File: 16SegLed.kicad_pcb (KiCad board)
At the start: 2 copper layers, 99.9 x 79.6 mm, 57 parts, among them J1 Conn_01x10, J2 Conn_01x10, J3 Conn_01x10, J4 Conn_01x06_Socket, J5 Conn_01x04_Pin, J6 Conn_01x04_Pin, Q1 BSS138, Q2 BSS138, SW1 SW_Push, SW2 SW_Push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

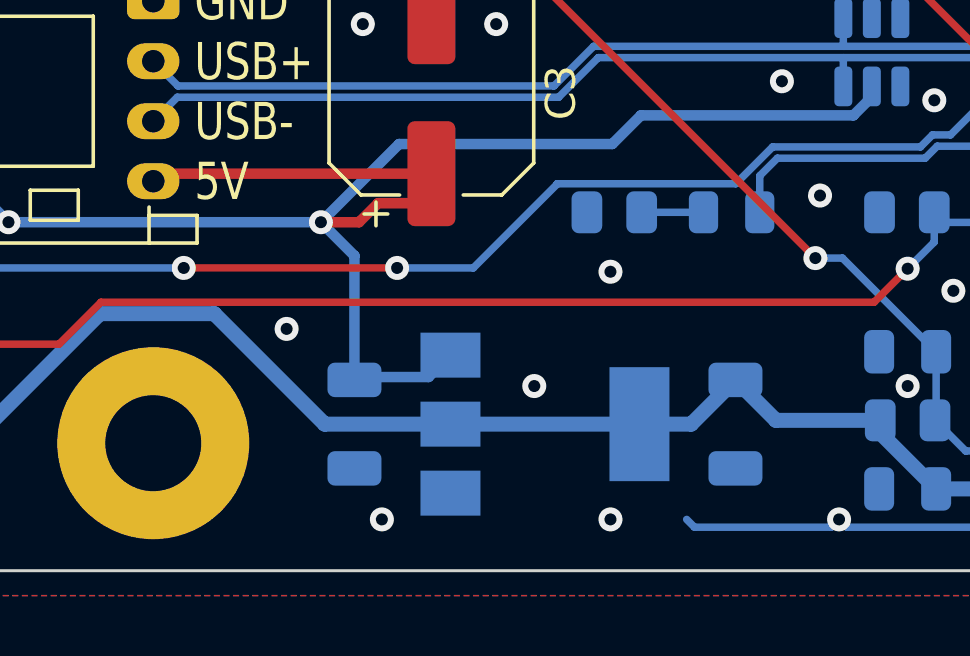
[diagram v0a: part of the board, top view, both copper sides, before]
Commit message: Fix 3.3 V regulator circuit
- Use polarized footprints for tantalum capacitors
- Add 100nF at input and output of AMS1117
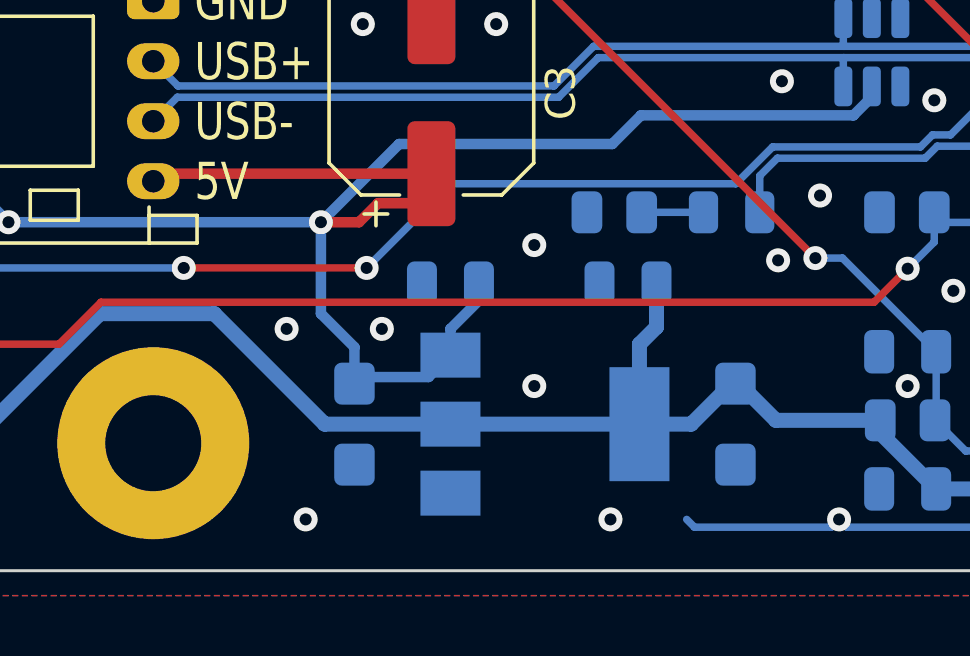
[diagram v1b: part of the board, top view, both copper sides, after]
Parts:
- added C10: 100nF, Capacitor_SMD:C_0805_2012Metric, B.Cu at (166.6, 163.2)
- added C11: 100nF, Capacitor_SMD:C_0805_2012Metric, B.Cu at (160.7, 163.2)
- C4, C5: footprint Capacitor_SMD:C_1206_3216Metric -> Capacitor_Tantalum_SMD:CP_EIA-3216-10_Kemet-I
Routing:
- net +3V3: track 121.5 -> 126.5 mm
- net +5V: track 200.0 -> 202.8 mm
- net GND: vias 96 -> 98

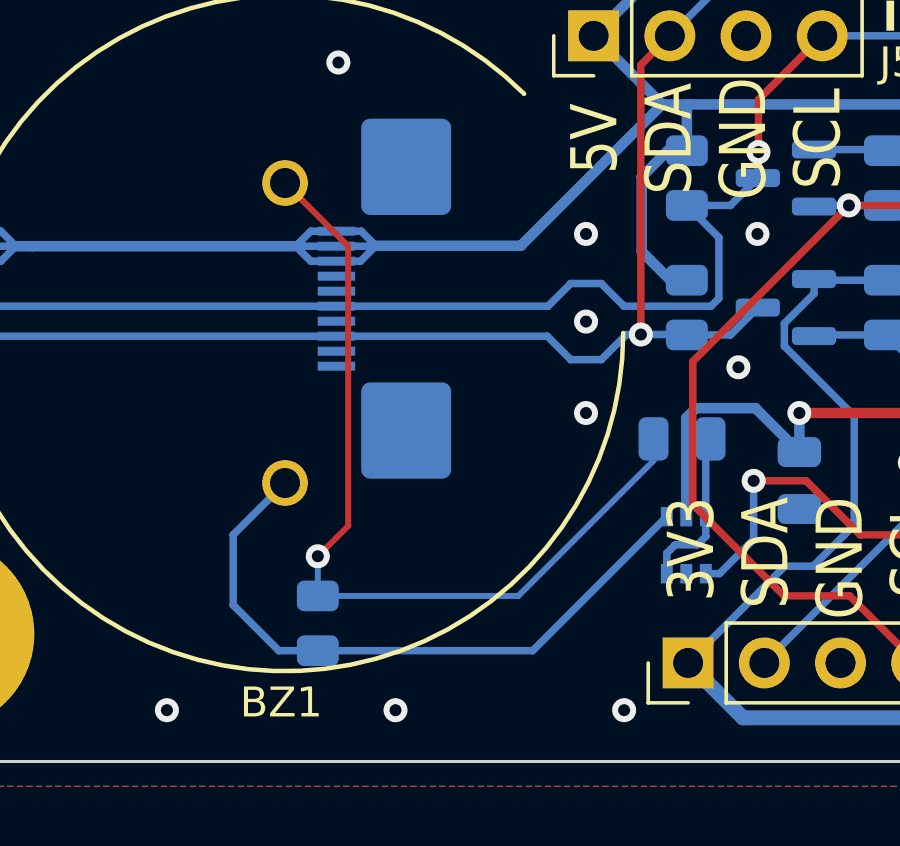
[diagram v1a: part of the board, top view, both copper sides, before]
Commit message: Add boxes to component groups on silkscreen
- including rearrangement of piezo buzzer's discharge resistor closer to other parts of that group
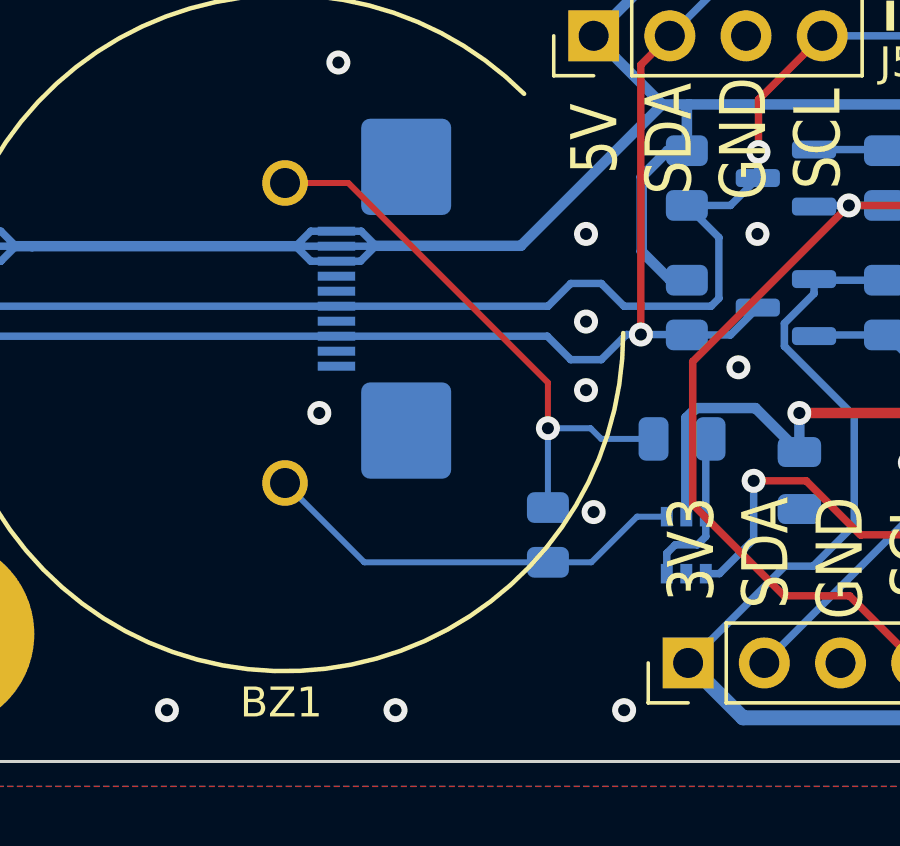
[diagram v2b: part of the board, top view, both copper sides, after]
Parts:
- moved R12 8.22 mm to (125.4, 165.3)
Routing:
- net /BZ-: track 28.8 -> 19.4 mm
- net /BZ+: track 21.7 -> 14.5 mm
- net GND: vias 98 -> 100
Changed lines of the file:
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@@
   )
   (footprint "Resistor_SMD:R_0805_2012Metric" (layer "B.Cu")
-    (at 117.7292 168.2244 90)
+    (at 125.4 165.278 90)
     (descr "Resistor SMD 0805 (2012 Metric), square (rectangular) end terminal, IPC_7351 nominal, (Body size source: IPC-SM-782 page 72, https://www.pcb-3d.com/wordpress/wp-content/uploads/ipc-sm-782a_amendment_1_and_2.pdf), generated with kicad-footprint-generator")
     (tags "resistor")
@@
     (property "ki_keywords" "R resistor")
     (attr smd)
-    (fp_text reference "R12" (at 0 -2.5146 180) (layer "B.SilkS")
+    (fp_text reference "R12" (at 2.286 0 180) (layer "B.SilkS")
         (effects (font (size 1 1) (thickness 0.15)) (justify mirror))
     )
@@
     (property "ki_keywords" "capacitor cap")
     (attr smd)
-    (fp_text reference "C9" (at 0 -1.9812 -360) (layer "B.SilkS")
+    (fp_text reference "C9" (at 2.3216 0 -360) (layer "B.SilkS")
         (effects (font (size 1 1) (thickness 0.15)) (justify mirror))
     )
@@
       (stroke (width 0.05) (type default)) (layer "B.CrtYd"))
   )
+  (gr_line (start 138.1 160.96) (end 123.622 160.96)
+    (stroke (width 0.15) (type default)) (layer "B.SilkS"))
+  (gr_line (start 171.882 172.39) (end 171.882 162.23)
+    (stroke (width 0.15) (type default)) (layer "B.SilkS"))
+  (gr_line (start 155.626 162.23) (end 155.626 172.39)
+    (stroke (width 0.15) (type default)) (layer "B.SilkS"))
   (gr_line (start 115.954238 151.7906) (end 107.953238 151.7906)
     (stroke (width 0.15) (type default)) (layer "B.SilkS"))
@@
   (gr_line (start 115.954238 156.3626) (end 107.953238 156.3626)
     (stroke (width 0.15) (type default)) (layer "B.SilkS"))
+  (gr_line (start 123.622 167.31) (end 123.622 160.96)
+    (stroke (width 0.15) (type default)) (layer "B.SilkS"))
+  (gr_line (start 138.1 150.038) (end 138.1 160.96)
+    (stroke (width 0.15) (type default)) (layer "B.SilkS"))
+  (gr_line (start 128.194 160.96) (end 128.194 150.038)
+    (stroke (width 0.15) (type default)) (layer "B.SilkS"))
   (gr_line (start 115.954238 162.7126) (end 115.954238 154.3306)
     (stroke (width 0.15) (type default)) (layer "B.SilkS"))
+  (gr_line (start 135.306 160.96) (end 135.306 167.31)
+    (stroke (width 0.15) (type default)) (layer "B.SilkS"))
   (gr_line (start 115.954238 162.7126) (end 107.953238 162.7126)
     (stroke (width 0.15) (type default)) (layer "B.SilkS"))
+  (gr_line (start 171.882 162.23) (end 155.626 162.23)
+    (stroke (width 0.15) (type default)) (layer "B.SilkS"))
   (gr_line (start 115.954238 159.9186) (end 107.953238 159.9186)
     (stroke (width 0.15) (type default)) (layer "B.SilkS"))
@@
   (gr_line (start 115.954238 154.5846) (end 107.953238 154.5846)
     (stroke (width 0.15) (type default)) (layer "B.SilkS"))
+  (gr_line (start 135.306 167.31) (end 123.622 167.31)
+    (stroke (width 0.15) (type default)) (layer "B.SilkS"))
+  (gr_line (start 128.194 150.038) (end 138.1 150.038)
+    (stroke (width 0.15) (type default)) (layer "B.SilkS"))
   (gr_arc (start 127.909673 158.547) (mid 106.222397 162.860867) (end 124.607982 150.576012)
     (stroke (width 0.15) (type default)) (layer "F.SilkS"))
@@
     )
   )
-  (gr_text "SCL\nG\nD\n3" (at 133.782 168.58 270) (layer "B.SilkS")
+  (gr_text "SCL\nG\nD\n3" (at 133.782 168.707 270) (layer "B.SilkS")
     (effects (font (size 1.54 1.3) (thickness 0.2)) (justify left mirror))
   )
@@
   (via (at 181.915 167.31) (size 0.8) (drill 0.4) (layers "F.Cu" "B.Cu") (free) (net 5))
   (via (at 190.17 103.175) (size 0.8) (drill 0.4) (layers "F.Cu" "B.Cu") (free) (net 5))
-  (via (at 126.67 161.214) (size 0.8) (drill 0.4) (layers "F.Cu" "B.Cu") (free) (net 5))
+  (via (at 126.67 160.452) (size 0.8) (drill 0.4) (layers "F.Cu" "B.Cu") (free) (net 5))
   (via (at 157.785 154.61) (size 0.8) (drill 0.4) (layers "F.Cu" "B.Cu") (free) (net 5))
   (via (at 199.06 166.04) (size 0.8) (drill 0.4) (layers "F.Cu" "B.Cu") (free) (net 5))
@@
   (via (at 199.06 163.5) (size 0.8) (drill 0.4) (layers "F.Cu" "B.Cu") (free) (net 5))
   (via (at 148.26 145.085) (size 0.8) (drill 0.4) (layers "F.Cu" "B.Cu") (free) (net 5))
+  (via (at 117.78 161.214) (size 0.8) (drill 0.4) (layers "F.Cu" "B.Cu") (free) (net 5))
   (via (at 139.37 153.34) (size 0.8) (drill 0.4) (layers "F.Cu" "B.Cu") (free) (net 5))
   (via (at 175.946 166.675) (size 0.8) (drill 0.4) (layers "F.Cu" "B.Cu") (free) (net 5))
@@
   (via (at 193.98 163.5) (size 0.8) (drill 0.4) (layers "F.Cu" "B.Cu") (free) (net 5))
   (via (at 144.45 132.385) (size 0.8) (drill 0.4) (layers "F.Cu" "B.Cu") (free) (net 5))
+  (via (at 126.924 164.516) (size 0.8) (drill 0.4) (layers "F.Cu" "B.Cu") (free) (net 5))
   (via (at 102.54 112.7) (size 0.8) (drill 0.4) (layers "F.Cu" "B.Cu") (free) (net 5))
   (via (at 188.9 100) (size 0.8) (drill 0.4) (layers "F.Cu" "B.Cu") (free) (net 5))
@@
   (segment (start 197.374382 154.168) (end 196.4135 154.168) (width 0.25) (layer "B.Cu") (net 90))
   (segment (start 196.52 156.14) (end 197.27 156.14) (width 0.25) (layer "B.Cu") (net 90))
-  (segment (start 124.8939 169.1369) (end 117.7292 169.1369) (width 0.25) (layer "B.Cu") (net 91))
-  (segment (start 114.9098 167.6148) (end 114.9098 165.274194) (width 0.25) (layer "B.Cu") (net 91))
-  (segment (start 114.9098 165.274194) (end 116.636994 163.547) (width 0.25) (layer "B.Cu") (net 91))
-  (segment (start 116.4319 169.1369) (end 114.9098 167.6148) (width 0.25) (layer "B.Cu") (net 91))
-  (segment (start 117.7292 169.1369) (end 116.4319 169.1369) (width 0.25) (layer "B.Cu") (net 91))
-  (segment (start 129.3624 164.6684) (end 124.8939 169.1369) (width 0.25) (layer "B.Cu") (net 91))
-  (segment (start 117.7292 165.9892) (end 118.7452 164.9732) (width 0.2) (layer "F.Cu") (net 92))
-  (segment (start 118.7452 155.655206) (end 116.636994 153.547) (width 0.2) (layer "F.Cu") (net 92))
-  (segment (start 118.7452 164.9732) (end 118.7452 155.655206) (width 0.2) (layer "F.Cu") (net 92))
-  (via (at 117.7292 165.9892) (size 0.8) (drill 0.4) (layers "F.Cu" "B.Cu") (net 92))
-  (segment (start 128.9204 162.8026) (end 124.4111 167.3119) (width 0.2) (layer "B.Cu") (net 92))
-  (segment (start 128.9204 162.0776) (end 128.9204 162.8026) (width 0.2) (layer "B.Cu") (net 92))
-  (segment (start 117.7292 167.3119) (end 117.7292 165.9892) (width 0.2) (layer "B.Cu") (net 92))
-  (segment (start 124.4111 167.3119) (end 117.7292 167.3119) (width 0.2) (layer "B.Cu") (net 92))
+  (segment (start 125.4 166.1905) (end 119.280494 166.1905) (width 0.2) (layer "B.Cu") (net 91))
+  (segment (start 119.280494 166.1905) (end 116.636994 163.547) (width 0.2) (layer "B.Cu") (net 91))
+  (segment (start 128.3699 164.6684) (end 126.8478 166.1905) (width 0.2) (layer "B.Cu") (net 91))
+  (segment (start 129.3624 164.6684) (end 128.3699 164.6684) (width 0.2) (layer "B.Cu") (net 91))
+  (segment (start 126.8478 166.1905) (end 125.4 166.1905) (width 0.2) (layer "B.Cu") (net 91))
+  (segment (start 118.749 153.547) (end 125.4 160.198) (width 0.2) (layer "F.Cu") (net 92))
+  (segment (start 116.636994 153.547) (end 118.749 153.547) (width 0.2) (layer "F.Cu") (net 92))
+  (segment (start 125.4 160.198) (end 125.4 161.722) (width 0.2) (layer "F.Cu") (net 92))
+  (via (at 125.4 161.722) (size 0.8) (drill 0.4) (layers "F.Cu" "B.Cu") (net 92))
+  (segment (start 125.4 161.722) (end 126.8224 161.722) (width 0.2) (layer "B.Cu") (net 92))
+  (segment (start 126.8224 161.722) (end 127.178 162.0776) (width 0.2) (layer "B.Cu") (net 92))
+  (segment (start 127.178 162.0776) (end 128.9204 162.0776) (width 0.2) (layer "B.Cu") (net 92))
+  (segment (start 125.4 161.722) (end 125.4 164.3655) (width 0.2) (layer "B.Cu") (net 92))
   (segment (start 130.3829 165.6083) (end 130.6624 165.3288) (width 0.25) (layer "B.Cu") (net 93))
   (segment (start 129.3624 165.8876) (end 129.6417 165.6083) (width 0.25) (layer "B.Cu") (net 93))

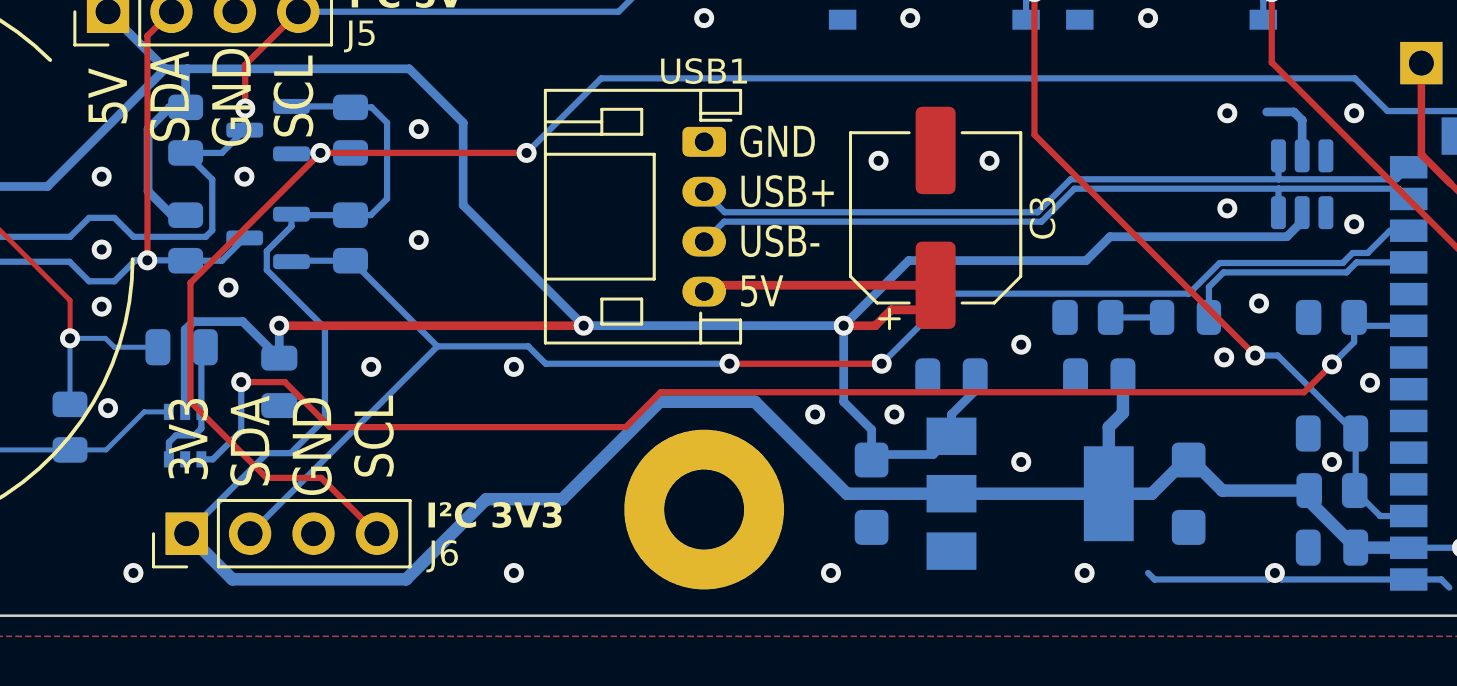
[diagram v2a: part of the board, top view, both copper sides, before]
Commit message: Rearrange I2C 3V3 testconnector into less crowded area on PCB
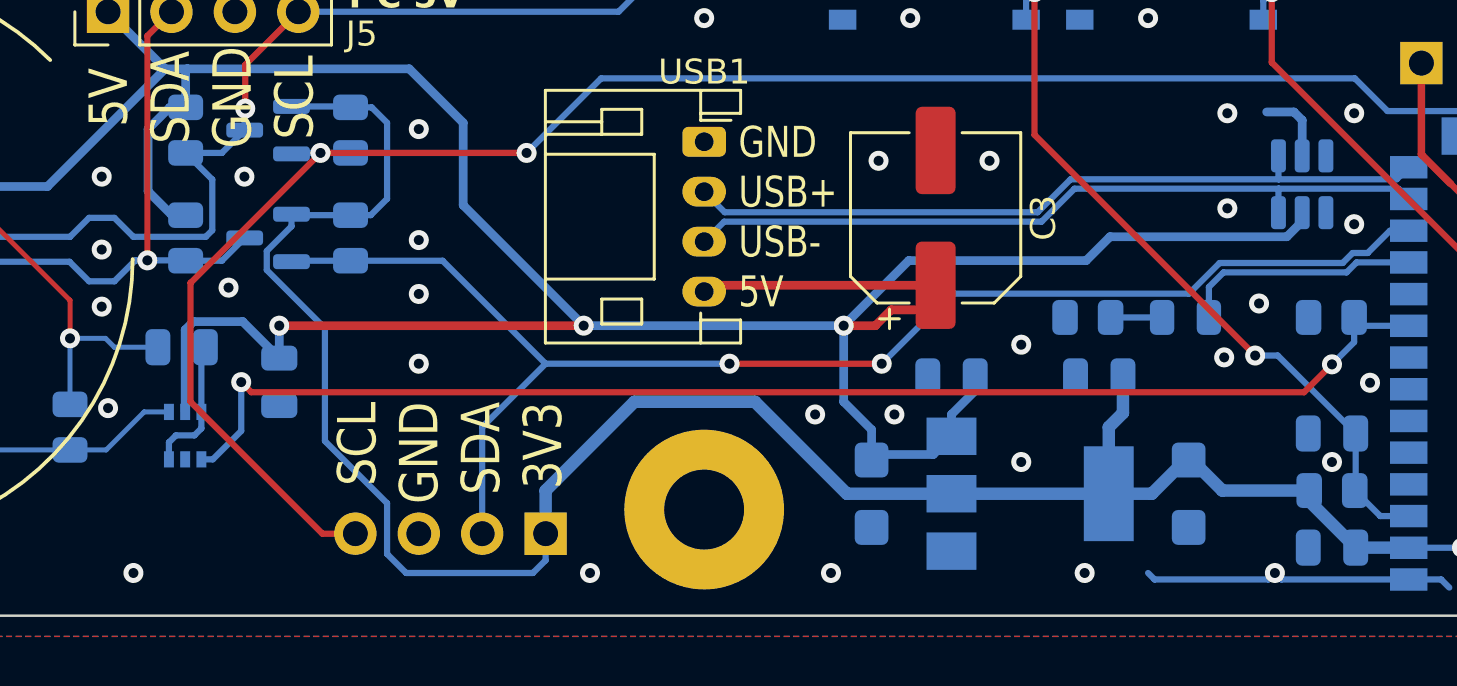
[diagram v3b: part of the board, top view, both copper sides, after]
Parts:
- J6: moved to B.Cu
- moved J6 14.4 mm to (144.4, 169.5)
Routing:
- net +3V3: track 126.5 -> 118.5 mm
- net /SDA3V3: track 59.3 -> 56.5 mm
- net /SND: track 54.1 -> 52.9 mm
- net /SCL3V3: track 74.8 -> 73.9 mm
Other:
- board text added: "SCL GND SDA 3V3"
- board text removed: "SCL G D 3"

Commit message: Update USB connectors to be able to move I2C 5V test connector to less crowded place
- using 2 of them (support installation on front and back in parallel in case needed differently in application than in prototype)
- using own footprint, matching LCSC part C5342444
- including own 3d model
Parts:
- added USB2: JST-PH2.0-4P, ProjectLibrary:PH 1x04 P2.0, B.Cu at (153.1, 156.8)
- J5: moved to B.Cu
- USB1: footprint Connector_JST:JST_PH_S4B-PH-K_1x04_P2.00mm_Horizontal -> ProjectLibrary:PH 1x04 P2.0
- moved J5 13.7 mm to (140.6, 148.6), turned to -90 degrees
- moved USB1 3.00 mm to (150.8, 156.8), turned to 90 degrees
- moved C11 0.08 mm to (160.7, 163.3)
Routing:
- net +5V: track 202.8 -> 191.6 mm
- net /SDA5V: track 95.2 -> 93.1 mm
- net GND: vias 100 -> 99
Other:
- board text removed: "GND USB+ USB- 5V"

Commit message: Include commit hash on PCB for first revision
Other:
- board text added: "Rev. 1.0 VCS: bc2069b6 Sascha Ruppert"
- board text removed: "Rev. 1.0 Sascha Ruppert"

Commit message: Support native USB-C
- use 6P terminal for wall mount USB-C socket
- include 2x 5k1 resistors for CC1 and CC2
- larger footprints of connectors require partial re-layout
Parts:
- added R15: 5.1kΩ, Resistor_SMD:R_0805_2012Metric, B.Cu at (147.8, 157.9)
- added R16: 5.1kΩ, Resistor_SMD:R_0805_2012Metric, B.Cu at (147.8, 155.9)
- USB1, USB2: value JST-PH2.0-4P -> HC-PH-6AW-G; footprint ProjectLibrary:PH 1x04 P2.0 -> ProjectLibrary:PH 1x06 P2.0
- moved SW2 24.6 mm to (194.0, 146.6)
- moved SW1 21.4 mm to (181.3, 146.6), turned to 180 degrees
- moved J5 13.7 mm to (127.0, 148.3)
- moved R14 2.46 mm to (168.6, 160.9)
- moved D3 2.21 mm to (172.3, 160.9)
- moved USB1 2.00 mm to (150.8, 154.8)
- moved USB2 2.00 mm to (153.1, 154.8)
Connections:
- USB1 pad 4: +5V -> /CC2
- USB2 pad 4: +5V -> /CC2
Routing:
- net /BOOT: track 32.0 -> 8.71 mm, vias 2 -> 0
- net /USB_D_MINUS: track 30.2 -> 50.4 mm
- net +5V: track 191.6 -> 206.1 mm
- net /CC1: track 0.00 -> 4.43 mm
- net /CC2: track 0.00 -> 4.43 mm
- net /SDA5V: track 93.1 -> 96.4 mm
- net /LED: track 9.63 -> 7.21 mm
- net GND: track 81.8 -> 79.8 mm, vias 99 -> 98
- net /SND: track 52.9 -> 54.8 mm
- net /IO35: track 6.44 -> 5.14 mm
- net /SCL5V: track 85.8 -> 87.1 mm
- net /CHIP_PU: track 29.7 -> 28.4 mm
- net /USB_D_PLUS: track 30.2 -> 30.8 mm
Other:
- board text added: "2024-JAN-__"
- board text added: "CL G DA 5V"
- board text added: "Rev. pre 1.1 VCS: ######## Sascha Ruppert"
- board text removed: "2024-JAN-07"
- board text removed: "Rev. 1.0 VCS: bc2069b6 Sascha Ruppert"
- board text removed: "SCL GND SDA 5V"
